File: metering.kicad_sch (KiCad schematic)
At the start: 42 parts, among them J1 Conn_01x08, J2 Conn_01x08, J3 USB_C_Receptacle_USB2.0_16P, J4 Prog, SW1 Reset, SW2 Boot, U1 USBLC6-2SC6, U2 AMS1117-3.3, U3 ESP32-C3-WROOM-02U, U4 74HC14, X1 Screw_Terminal_01x06, X2 Screw_Terminal_01x06, Y1 32.768kHz

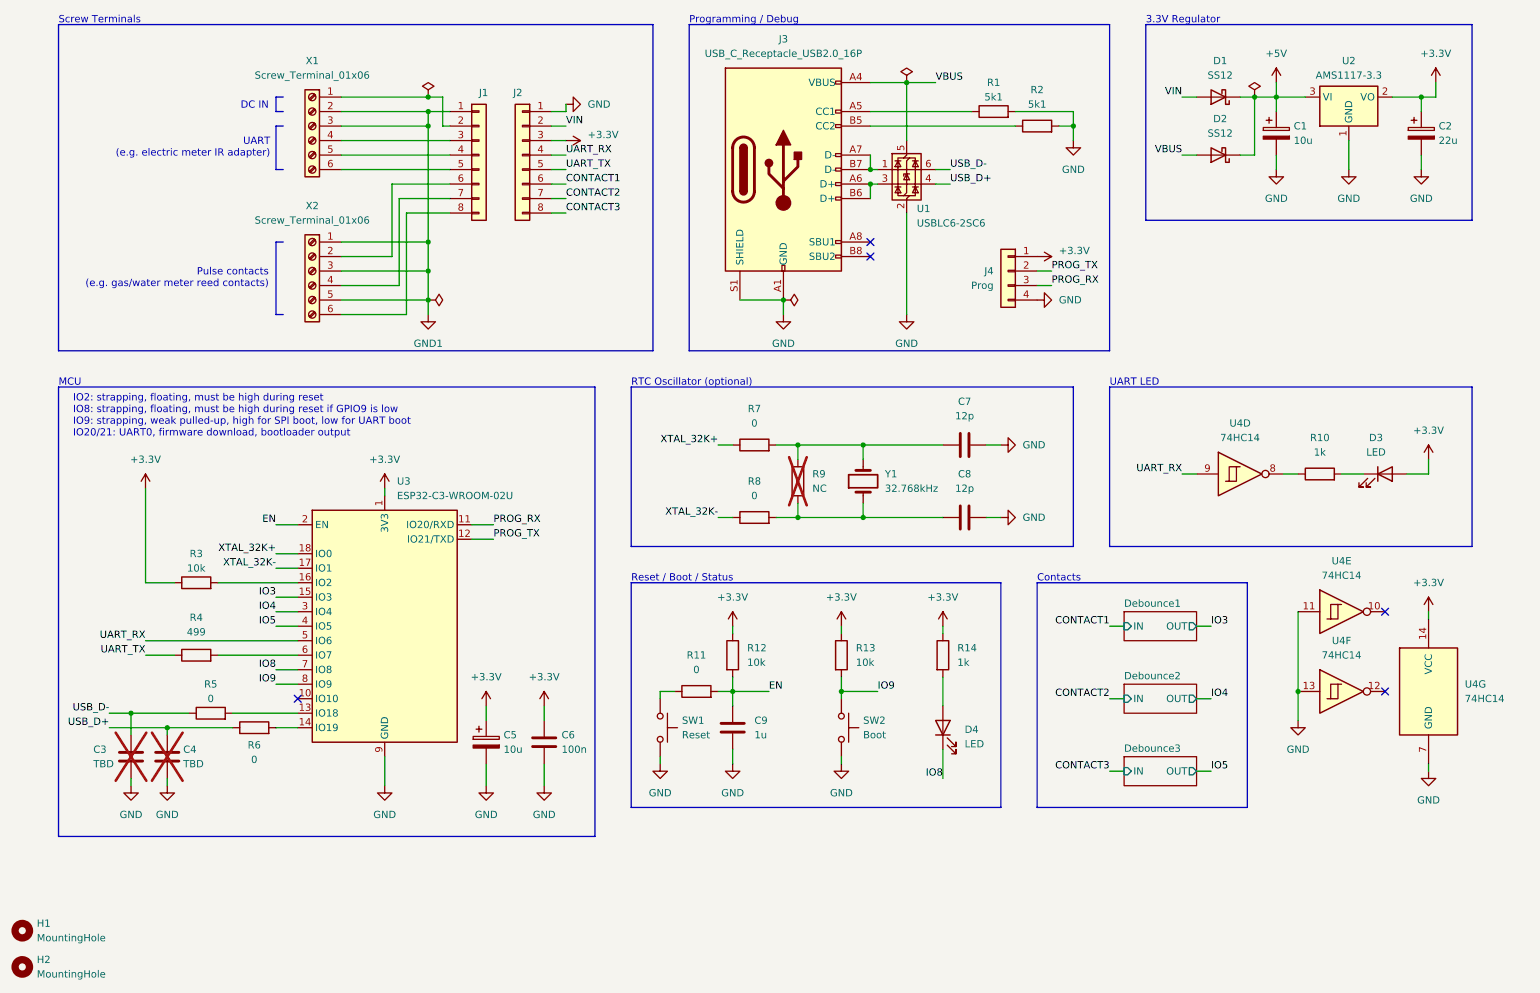
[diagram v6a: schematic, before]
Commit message: Improve schematic style
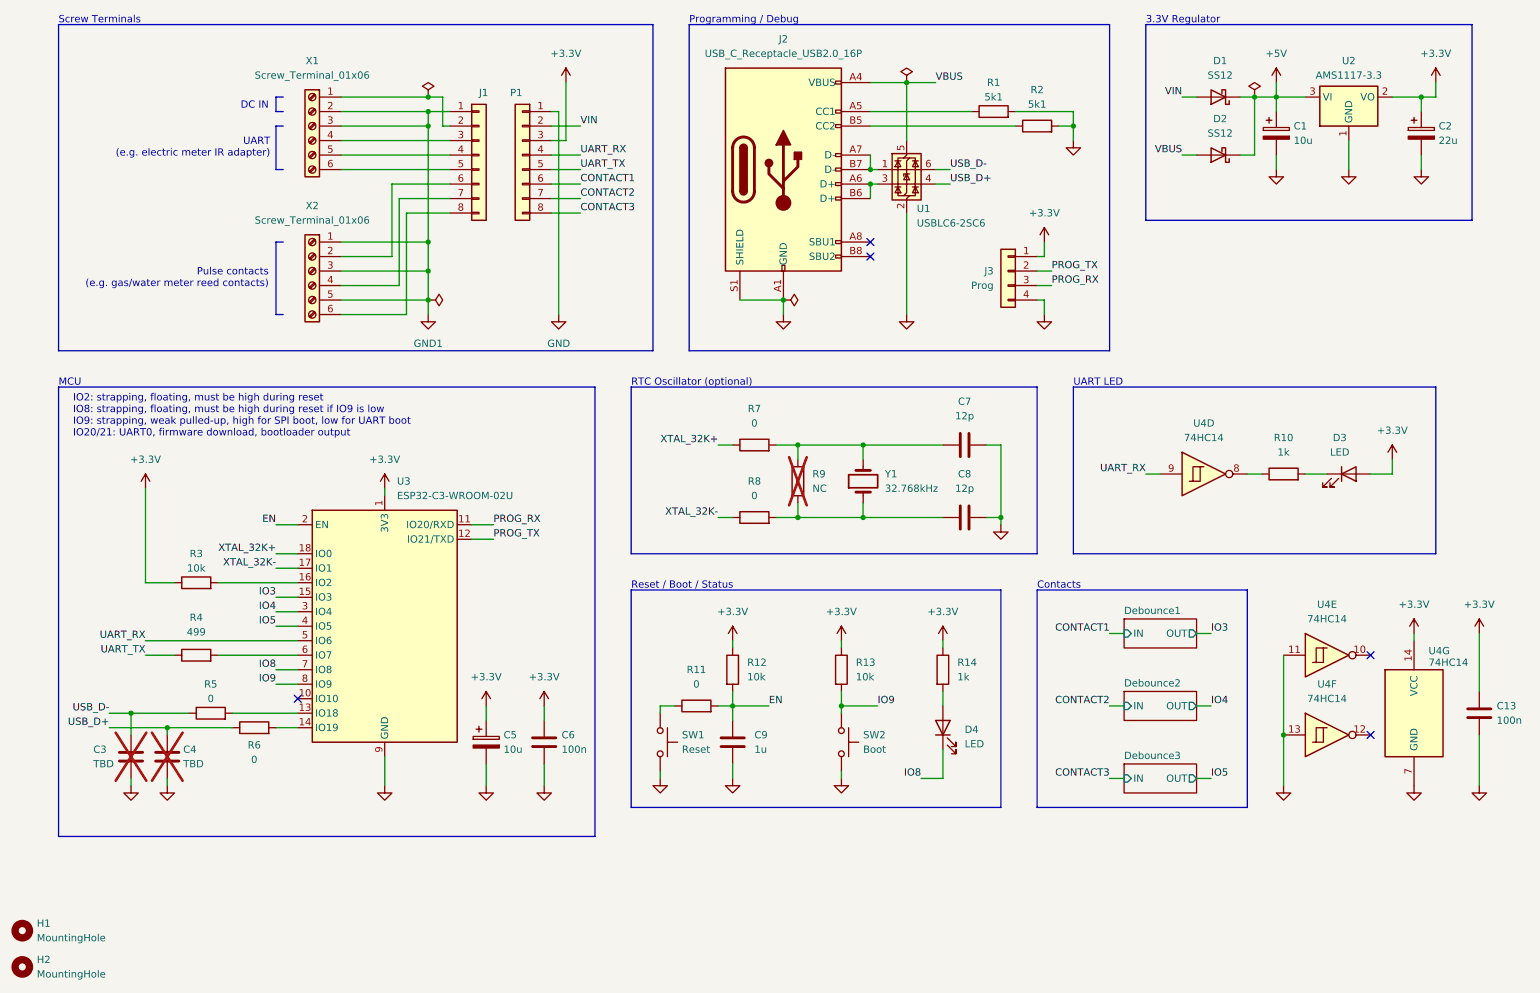
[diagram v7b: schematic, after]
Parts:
- added C13: 100n, Capacitor_SMD:C_0805_2012Metric, symbol Device:C
- SW1, SW2: footprint Button_Switch_SMD:SW_SPST_PTS647_Sx38 -> Button_Switch_SMD:SW_Tactile_SPST_NO_Straight_CK_PTS636Sx25SMTRLFS
- renumbered J3 to J2, J4 to J3, J2 to P1
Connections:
- net +3.3V: now also C13.1
- net GND: now also C13.2
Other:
- note added: "IO2: strapping, floating, must be high during reset IO8: strapping, floating, must be high during reset if IO9 is low IO9: strapping, weak pulled-up, high for SPI boot, low for UART boot IO20/21: UART0, firmware download, bootloader output"
- note removed: "IO2: strapping, floating, must be high during reset IO8: strapping, floating, must be high during reset if GPIO9 is low IO9: strapping, weak pulled-up, high for SPI boot, low for UART boot IO20/21: UART0, firmware download, bootloader output"
- moved on the sheet: C9, D3, R10, R11, R12, R13, R14, SW1, SW2, U4D, U4E, U4F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
